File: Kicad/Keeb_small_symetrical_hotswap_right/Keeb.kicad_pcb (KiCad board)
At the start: 2 copper layers, 96.2 x 98.1 mm, 32 parts, among them J1 TYPE-C-31-M-12, J2 B2B-XH-A_LF__SN_, SW1 CherryMX, SW10 CherryMX, SW11 CherryMX, SW13 CherryMX, SW14 CherryMX, SW15 CherryMX, SW16 CherryMX, SW17 CherryMX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

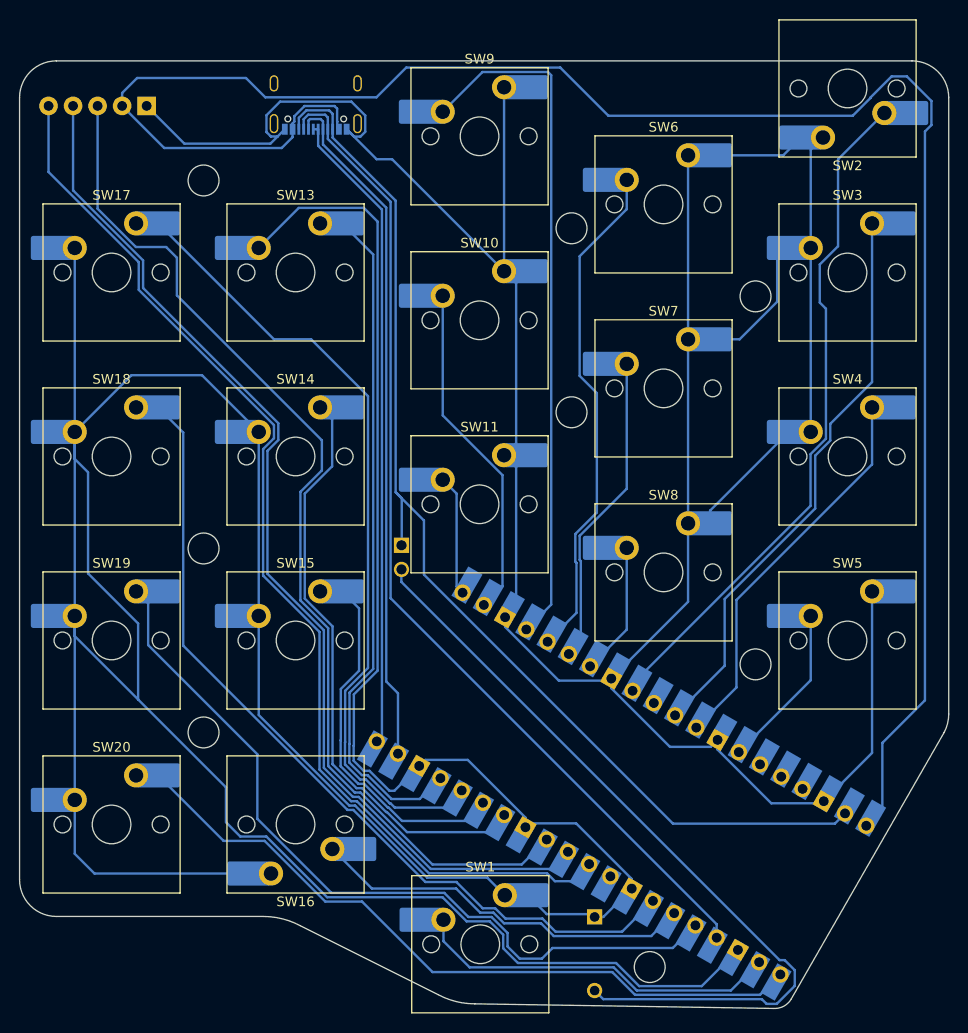
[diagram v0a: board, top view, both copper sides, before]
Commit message: Implemented encoders on the split halves
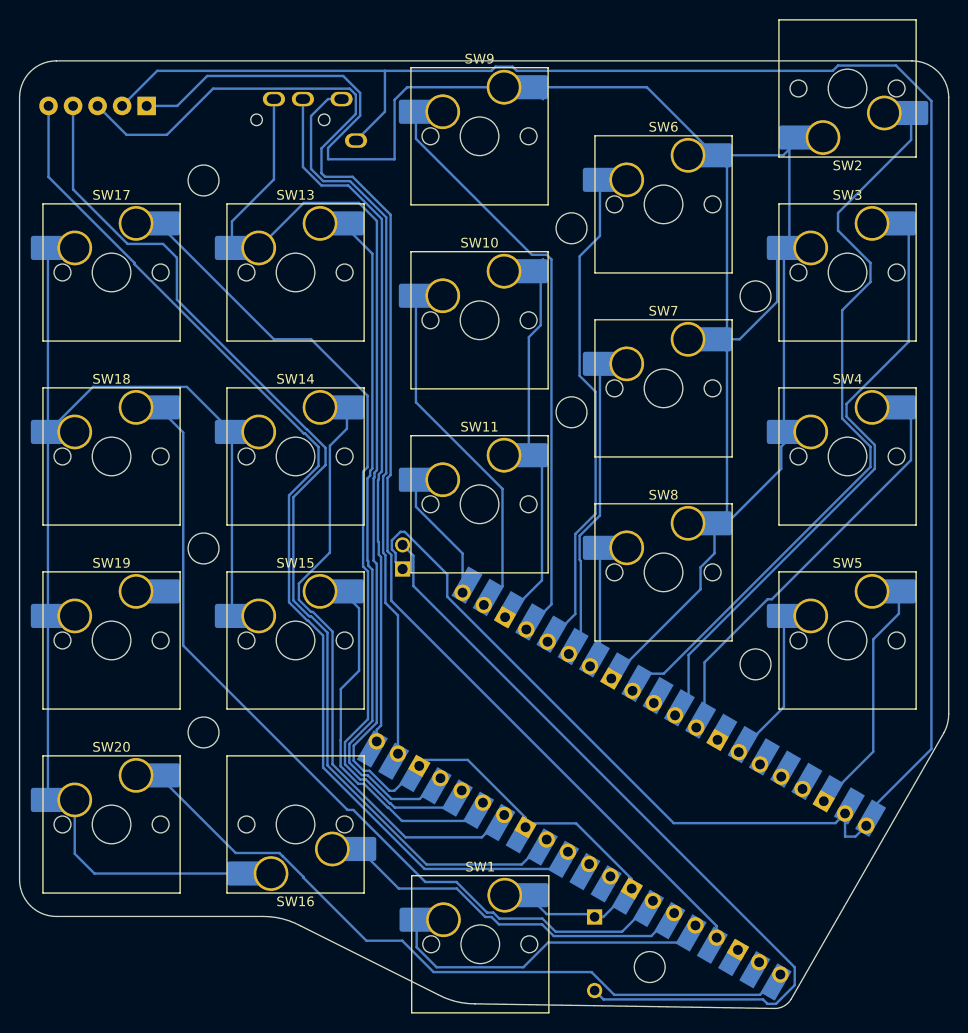
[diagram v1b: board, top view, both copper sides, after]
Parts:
- removed J1: TYPE-C-31-M-12, TypeC:HRO_TYPE-C-31-M-12
- added J3: MJ-4PP-9_MJ-4PP-9, MJ-4PP-9:MJ-4PP-9_no_silk, F.Cu at (131.7, 39.8)
- SW1, SW10, SW11, SW13, SW14, SW15, SW16, SW17, SW18, SW19, SW2, SW20, SW3, SW4, SW5, SW6, SW7, SW8, SW9: footprint ScottoKeebs_Hotswap:Hotswap_MX_Plated_1.00u_Smaller_hole -> ScottoKeebs_Hotswap:Hotswap_MX_Plated_1.00u
- moved J2 0.94 mm to (141.7, 85.1), turned to -90 degrees
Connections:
- J2 pad 1: VSYS -> 3v3
- SW1 pad 1: 1 -> 3
- SW19 pad 2: 3 -> 1
- U1 pad 39: VSYS -> 3v3
- U2 pad CLK: 7 -> 8
- U2 pad DT: 8 -> 9
- U2 pad SW: 9 -> 2
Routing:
- net GND: track 719.6 -> 544.1 mm
- net VSYS: track 117.1 -> 0.00 mm
- net 7: track 114.7 -> 0.00 mm
- net 3: track 82.3 -> 34.4 mm
- net 3v3: track 199.9 -> 243.5 mm
- net 1: track 38.2 -> 0.00 mm
- net 2: track 105.5 -> 137.8 mm
- net 18: track 71.5 -> 61.4 mm
- net 22: track 71.2 -> 77.8 mm
- net 15: track 66.8 -> 72.0 mm
- net 26: track 59.4 -> 63.8 mm
- net 14: track 71.3 -> 75.5 mm
- net 27: track 40.7 -> 44.7 mm
- net 8: track 110.6 -> 113.4 mm
- net 4: track 40.1 -> 37.3 mm
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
